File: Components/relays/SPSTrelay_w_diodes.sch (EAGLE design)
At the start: 3 parts, among them K1 PY14-02

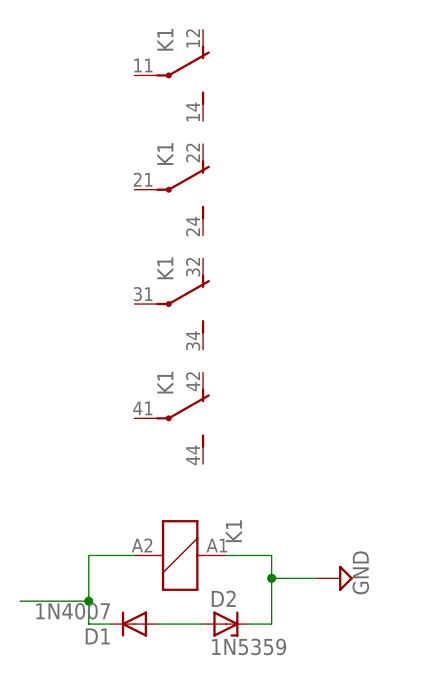
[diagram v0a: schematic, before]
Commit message: Creating re-usable suppressed relay components w/ vertical diodes
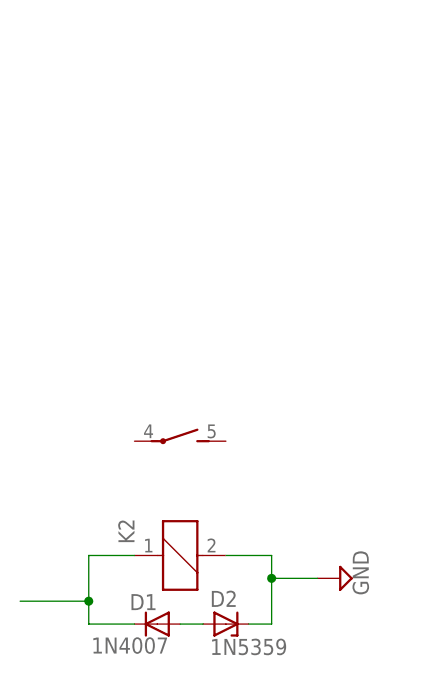
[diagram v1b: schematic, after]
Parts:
- removed K1: PY14-02, relay_computer_custom:PY14-02
- added K2: HF41F-12-H, relay_computer_custom:HF41F-12-H
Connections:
- net GND: now also K21.2; no longer K11.1
- net IN: now also K21.1; no longer K11.2
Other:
- moved on the sheet: D1
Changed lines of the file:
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@@
 </classes>
 <parts>
-<part name="K1" library="relay_computer_custom" deviceset="PY14-02" device=""/>
 <part name="SUPPLY1" library="supply2" library_urn="urn:adsk.eagle:library:372" deviceset="GND" device=""/>
 <part name="D1" library="relay_computer_custom" deviceset="1N4007" device=""/>
 <part name="D2" library="relay_computer_custom" deviceset="1N5359" device=""/>
+<part name="K2" library="relay_computer_custom" deviceset="HF41F-12-H" device=""/>
 </parts>
 <sheets>
@@
 </plain>
 <instances>
-<instance part="K1" gate="1" x="17.78" y="15.24" rot="MR90"/>
-<instance part="K1" gate="2" x="15.24" y="68.58" rot="MR90"/>
-<instance part="K1" gate="3" x="15.24" y="55.88" rot="MR90"/>
-<instance part="K1" gate="4" x="15.24" y="43.18" rot="MR90"/>
-<instance part="K1" gate="5" x="15.24" y="30.48" rot="MR90"/>
 <instance part="SUPPLY1" gate="GND" x="35.56" y="12.7" rot="R90"/>
-<instance part="D1" gate="1" x="12.7" y="7.62" rot="R180"/>
+<instance part="D1" gate="1" x="15.24" y="7.62" smashed="yes" rot="R180">
+<attribute name="NAME" x="15.24" y="10.9474" size="1.778" layer="95" rot="R180"/>
+<attribute name="VALUE" x="16.51" y="6.1214" size="1.778" layer="96" rot="R180"/>
+</instance>
 <instance part="D2" gate="1" x="22.86" y="7.62"/>
+<instance part="K2" gate="1" x="17.78" y="15.24" rot="R90"/>
+<instance part="K2" gate="G$1" x="17.78" y="27.94" rot="R270"/>
 </instances>
 <busses>
@@
 <net name="D$1" class="0">
 <segment>
+<wire x1="17.78" y1="7.62" x2="20.32" y2="7.62" width="0.1524" layer="91"/>
 <pinref part="D1" gate="1" pin="A"/>
 <pinref part="D2" gate="1" pin="A"/>
-<wire x1="15.24" y1="7.62" x2="20.32" y2="7.62" width="0.1524" layer="91"/>
 </segment>
 </net>
 <net name="GND" class="0">
 <segment>
-<pinref part="K1" gate="1" pin="1"/>
 <wire x1="22.86" y1="15.24" x2="27.94" y2="15.24" width="0.1524" layer="91"/>
 <wire x1="27.94" y1="15.24" x2="27.94" y2="12.7" width="0.1524" layer="91"/>
-<pinref part="D2" gate="1" pin="C"/>
 <wire x1="27.94" y1="12.7" x2="27.94" y2="7.62" width="0.1524" layer="91"/>
 <wire x1="25.4" y1="7.62" x2="27.94" y2="7.62" width="0.1524" layer="91"/>
@@
 <wire x1="27.94" y1="12.7" x2="33.02" y2="12.7" width="0.1524" layer="91"/>
 <junction x="27.94" y="12.7"/>
+<pinref part="D2" gate="1" pin="C"/>
+<pinref part="K2" gate="1" pin="2"/>
 </segment>
 </net>
 <net name="IN" class="0">
 <segment>
-<pinref part="K1" gate="1" pin="2"/>
 <wire x1="12.7" y1="15.24" x2="7.62" y2="15.24" width="0.1524" layer="91"/>
 <wire x1="7.62" y1="15.24" x2="7.62" y2="10.16" width="0.1524" layer="91"/>
 <wire x1="7.62" y1="10.16" x2="0" y2="10.16" width="0.1524" layer="91"/>
 <junction x="7.62" y="10.16"/>
+<wire x1="12.7" y1="7.62" x2="7.62" y2="7.62" width="0.1524" layer="91"/>
+<wire x1="7.62" y1="7.62" x2="7.62" y2="10.16" width="0.1524" layer="91"/>
 <pinref part="D1" gate="1" pin="C"/>
-<wire x1="10.16" y1="7.62" x2="7.62" y2="7.62" width="0.1524" layer="91"/>
-<wire x1="7.62" y1="7.62" x2="7.62" y2="10.16" width="0.1524" layer="91"/>
+<pinref part="K2" gate="1" pin="1"/>
 </segment>
 </net>

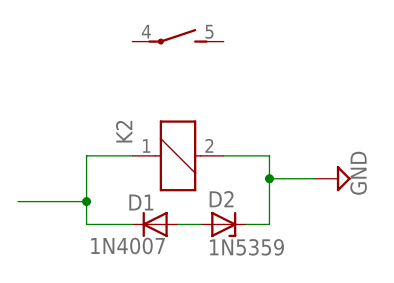
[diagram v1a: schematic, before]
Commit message: Correcting footprint for SPST and SPDT relays
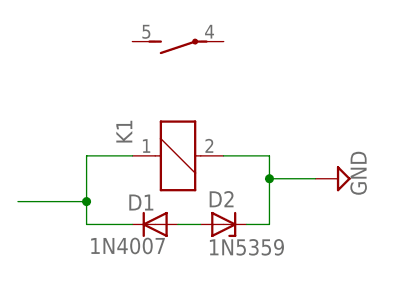
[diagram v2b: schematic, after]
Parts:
- renumbered K2 to K1
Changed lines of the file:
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@@
 <?xml version="1.0" encoding="utf-8"?>
 <!DOCTYPE eagle SYSTEM "eagle.dtd">
-<eagle version="8.3.2">
+<eagle version="8.7.0">
 <drawing>
 <settings>
-<setting alwaysvectorfont="no"/>
+<setting alwaysvectorfont="yes"/>
 <setting keepoldvectorfont="yes"/>
 <setting verticaltext="up"/>
@@
 <part name="D1" library="relay_computer_custom" deviceset="1N4007" device=""/>
 <part name="D2" library="relay_computer_custom" deviceset="1N5359" device=""/>
-<part name="K2" library="relay_computer_custom" deviceset="HF41F-12-H" device=""/>
+<part name="K1" library="relay_computer_custom" deviceset="HF41F-12-H" device=""/>
 </parts>
 <sheets>
@@
 </instance>
 <instance part="D2" gate="1" x="22.86" y="7.62"/>
-<instance part="K2" gate="1" x="17.78" y="15.24" rot="R90"/>
-<instance part="K2" gate="G$1" x="17.78" y="27.94" rot="R270"/>
+<instance part="K1" gate="1" x="17.78" y="15.24" rot="R90"/>
+<instance part="K1" gate="G$1" x="17.78" y="27.94" rot="R90"/>
 </instances>
 <busses>
@@
 <junction x="27.94" y="12.7"/>
 <pinref part="D2" gate="1" pin="C"/>
-<pinref part="K2" gate="1" pin="2"/>
+<pinref part="K1" gate="1" pin="2"/>
 </segment>
 </net>
@@
 <wire x1="7.62" y1="7.62" x2="7.62" y2="10.16" width="0.1524" layer="91"/>
 <pinref part="D1" gate="1" pin="C"/>
-<pinref part="K2" gate="1" pin="1"/>
+<pinref part="K1" gate="1" pin="1"/>
 </segment>
 </net>

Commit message: Updating components with latest library updates
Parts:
- D2: value 1N5359 -> 1N5359VERT_SML; device relay_computer_custom:1N5359 -> relay_computer_custom:1N5359VERT_SML
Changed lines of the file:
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@@
 <layer number="48" name="Document" color="7" fill="1" visible="no" active="no"/>
 <layer number="49" name="Reference" color="7" fill="1" visible="no" active="no"/>
+<layer number="50" name="dxf" color="7" fill="1" visible="no" active="no"/>
 <layer number="51" name="tDocu" color="6" fill="1" visible="no" active="no"/>
 <layer number="52" name="bDocu" color="7" fill="1" visible="no" active="no"/>
+<layer number="53" name="tGND_GNDA" color="7" fill="9" visible="no" active="no"/>
+<layer number="54" name="bGND_GNDA" color="1" fill="9" visible="no" active="no"/>
+<layer number="56" name="wert" color="7" fill="1" visible="no" active="no"/>
+<layer number="57" name="tCAD" color="7" fill="1" visible="no" active="no"/>
+<layer number="59" name="tCarbon" color="7" fill="1" visible="no" active="no"/>
+<layer number="60" name="bCarbon" color="7" fill="1" visible="no" active="no"/>
 <layer number="90" name="Modules" color="5" fill="1" visible="yes" active="yes"/>
 <layer number="91" name="Nets" color="2" fill="1" visible="yes" active="yes"/>
@@
 <layer number="98" name="Guide" color="6" fill="1" visible="yes" active="yes"/>
 <layer number="99" name="SpiceOrder" color="5" fill="1" visible="yes" active="yes"/>
+<layer number="100" name="Muster" color="7" fill="1" visible="no" active="no"/>
+<layer number="101" name="Patch_Top" color="12" fill="4" visible="no" active="yes"/>
+<layer number="102" name="Vscore" color="7" fill="1" visible="no" active="yes"/>
+<layer number="103" name="fp3" color="7" fill="1" visible="no" active="yes"/>
+<layer number="104" name="Name" color="7" fill="1" visible="no" active="yes"/>
+<layer number="105" name="Beschreib" color="9" fill="1" visible="no" active="yes"/>
+<layer number="106" name="BGA-Top" color="4" fill="1" visible="no" active="yes"/>
+<layer number="107" name="BD-Top" color="5" fill="1" visible="no" active="yes"/>
+<layer number="108" name="fp8" color="7" fill="1" visible="no" active="yes"/>
+<layer number="109" name="fp9" color="7" fill="1" visible="no" active="yes"/>
+<layer number="110" name="fp0" color="7" fill="1" visible="no" active="yes"/>
+<layer number="111" name="LPC17xx" color="7" fill="1" visible="no" active="yes"/>
+<layer number="112" name="tSilk" color="7" fill="1" visible="no" active="yes"/>
+<layer number="113" name="ReferenceLS" color="7" fill="1" visible="no" active="no"/>
+<layer number="114" name="Badge_Outline" color="7" fill="1" visible="no" active="yes"/>
+<layer number="115" name="ReferenceISLANDS" color="7" fill="1" visible="no" active="yes"/>
+<layer number="116" name="Patch_BOT" color="9" fill="4" visible="no" active="yes"/>
+<layer number="118" name="Rect_Pads" color="7" fill="1" visible="no" active="no"/>
+<layer number="121" name="_tsilk" color="7" fill="1" visible="no" active="yes"/>
+<layer number="122" name="_bsilk" color="7" fill="1" visible="no" active="yes"/>
+<layer number="123" name="tTestmark" color="7" fill="1" visible="no" active="yes"/>
+<layer number="124" name="bTestmark" color="7" fill="1" visible="no" active="yes"/>
+<layer number="125" name="_tNames" color="7" fill="1" visible="no" active="yes"/>
+<layer number="126" name="_bNames" color="7" fill="1" visible="no" active="yes"/>
+<layer number="127" name="_tValues" color="7" fill="1" visible="no" active="yes"/>
+<layer number="128" name="_bValues" color="7" fill="1" visible="no" active="yes"/>
+<layer number="129" name="Mask" color="7" fill="1" visible="no" active="yes"/>
+<layer number="131" name="tAdjust" color="7" fill="1" visible="no" active="yes"/>
+<layer number="132" name="bAdjust" color="7" fill="1" visible="no" active="yes"/>
+<layer number="144" name="Drill_legend" color="7" fill="1" visible="no" active="yes"/>
+<layer number="150" name="Notes" color="7" fill="1" visible="no" active="yes"/>
+<layer number="151" name="HeatSink" color="7" fill="1" visible="no" active="yes"/>
+<layer number="152" name="_bDocu" color="7" fill="1" visible="no" active="yes"/>
+<layer number="153" name="FabDoc1" color="6" fill="1" visible="no" active="no"/>
+<layer number="154" name="FabDoc2" color="2" fill="1" visible="no" active="no"/>
+<layer number="155" name="FabDoc3" color="7" fill="15" visible="no" active="no"/>
+<layer number="199" name="Contour" color="7" fill="1" visible="no" active="yes"/>
+<layer number="200" name="200bmp" color="1" fill="10" visible="no" active="yes"/>
+<layer number="201" name="201bmp" color="2" fill="1" visible="no" active="no"/>
+<layer number="202" name="202bmp" color="3" fill="1" visible="no" active="no"/>
+<layer number="203" name="203bmp" color="4" fill="10" visible="no" active="yes"/>
+<layer number="204" name="204bmp" color="5" fill="10" visible="no" active="yes"/>
+<layer number="205" name="205bmp" color="6" fill="10" visible="no" active="yes"/>
+<layer number="206" name="206bmp" color="7" fill="10" visible="no" active="yes"/>
+<layer number="207" name="207bmp" color="8" fill="10" visible="no" active="yes"/>
+<layer number="208" name="208bmp" color="9" fill="10" visible="no" active="yes"/>
+<layer number="209" name="209bmp" color="7" fill="1" visible="no" active="yes"/>
+<layer number="210" name="210bmp" color="7" fill="1" visible="no" active="yes"/>
+<layer number="211" name="211bmp" color="7" fill="1" visible="no" active="yes"/>
+<layer number="212" name="212bmp" color="7" fill="1" visible="no" active="yes"/>
+<layer number="213" name="213bmp" color="7" fill="1" visible="no" active="yes"/>
+<layer number="214" name="214bmp" color="7" fill="1" visible="no" active="yes"/>
+<layer number="215" name="215bmp" color="7" fill="1" visible="no" active="yes"/>
+<layer number="216" name="216bmp" color="7" fill="1" visible="no" active="yes"/>
+<layer number="217" name="217bmp" color="18" fill="1" visible="no" active="no"/>
+<layer number="218" name="218bmp" color="19" fill="1" visible="no" active="no"/>
+<layer number="219" name="219bmp" color="20" fill="1" visible="no" active="no"/>
+<layer number="220" name="220bmp" color="21" fill="1" visible="no" active="no"/>
+<layer number="221" name="221bmp" color="22" fill="1" visible="no" active="no"/>
+<layer number="222" name="222bmp" color="23" fill="1" visible="no" active="no"/>
+<layer number="223" name="223bmp" color="24" fill="1" visible="no" active="no"/>
+<layer number="224" name="224bmp" color="25" fill="1" visible="no" active="no"/>
+<layer number="225" name="225bmp" color="7" fill="1" visible="no" active="yes"/>
+<layer number="226" name="226bmp" color="7" fill="1" visible="no" active="yes"/>
+<layer number="227" name="227bmp" color="7" fill="1" visible="no" active="yes"/>
+<layer number="228" name="228bmp" color="7" fill="1" visible="no" active="yes"/>
+<layer number="229" name="229bmp" color="7" fill="1" visible="no" active="yes"/>
+<layer number="230" name="230bmp" color="7" fill="1" visible="no" active="yes"/>
+<layer number="231" name="Eagle3D_PG1" color="7" fill="1" visible="no" active="no"/>
+<layer number="232" name="Eagle3D_PG2" color="7" fill="1" visible="no" active="no"/>
+<layer number="233" name="Eagle3D_PG3" color="7" fill="1" visible="no" active="no"/>
+<layer number="248" name="Housing" color="7" fill="1" visible="no" active="yes"/>
+<layer number="249" name="Edge" color="7" fill="1" visible="no" active="yes"/>
+<layer number="250" name="Descript" color="7" fill="1" visible="no" active="no"/>
+<layer number="251" name="SMDround" color="7" fill="1" visible="no" active="no"/>
+<layer number="254" name="cooling" color="7" fill="1" visible="no" active="yes"/>
+<layer number="255" name="routoute" color="7" fill="1" visible="no" active="yes"/>
 </layers>
 <schematic xreflabel="%F%N/%S.%C%R" xrefpart="/%S.%C%R">
@@
 <part name="SUPPLY1" library="supply2" library_urn="urn:adsk.eagle:library:372" deviceset="GND" device=""/>
 <part name="D1" library="relay_computer_custom" deviceset="1N4007" device=""/>
-<part name="D2" library="relay_computer_custom" deviceset="1N5359" device=""/>
+<part name="D2" library="relay_computer_custom" deviceset="1N5359" device="VERT_SML"/>
 <part name="K1" library="relay_computer_custom" deviceset="HF41F-12-H" device=""/>
 </parts>
